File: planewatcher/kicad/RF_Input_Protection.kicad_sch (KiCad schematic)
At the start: 2 parts

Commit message: Add persistent PCBWay BOM fields to KiCad schematic
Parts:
- D3: MPN (none) -> ESD103B102ELE6327XTMA1; Manufacturer (none) -> Infineon; Package (none) -> PG-TSLP-2-20
- L12: MPN (none) -> 0402DC-68NXJRW; Manufacturer (none) -> Coilcraft; Package (none) -> 0402
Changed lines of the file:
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@@
+			)
+		)
+		(property "Package" "PG-TSLP-2-20"
+			(at 139.7 97.79 0)
+			(hide yes)
+			(show_name no)
+			(do_not_autoplace no)
+			(effects
+				(font
+					(size 1.27 1.27)
+				)
+			)
+		)
+		(property "MPN" "ESD103B102ELE6327XTMA1"
+			(at 139.7 97.79 0)
+			(hide yes)
+			(show_name no)
+			(do_not_autoplace no)
+			(effects
+				(font
+					(size 1.27 1.27)
+				)
+			)
+		)
+		(property "Manufacturer" "Infineon"
+			(at 139.7 97.79 0)
+			(hide yes)
+			(show_name no)
+			(do_not_autoplace no)
+			(effects
+				(font
+					(size 1.27 1.27)
+				)
 			)
 		)
@@
 			(at 123.19 97.79 0)
 			(hide yes)
+			(show_name no)
+			(do_not_autoplace no)
+			(effects
+				(font
+					(size 1.27 1.27)
+				)
+			)
+		)
+		(property "Package" "0402"
+			(at 123.19 97.79 0)
+			(hide yes)
+			(show_name no)
+			(do_not_autoplace no)
+			(effects
+				(font
+					(size 1.27 1.27)
+				)
+			)
+		)
+		(property "MPN" "0402DC-68NXJRW"
+			(at 123.19 97.79 0)
+			(hide yes)
+			(show_name no)
+			(do_not_autoplace no)
+			(effects
+				(font
+					(size 1.27 1.27)
+				)
+			)
+		)
+		(property "Manufacturer" "Coilcraft"
+			(at 123.19 97.79 0)
+			(hide yes)

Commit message: move power supply and add GPS module
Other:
- title: Plane Watcher: RF Input Protection -> Plane Watcher
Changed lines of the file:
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@@
 	(paper "A4")
 	(title_block
-		(title "Plane Watcher: RF Input Protection")
-		(date "2026-05-16")
-		(rev "prototype 1.1")
+		(title "Plane Watcher")
+		(date "2026-05-18")
+		(rev "prototype 1.2")
 		(company "plane.watch")
 	)

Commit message: review & consolidate all capacitors
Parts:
- D3: Suggested Part Infineon ESD103B102ELE6327XTMA1 -> (none)
- L12: Suggested Part Coilcraft 0402DC-68NXJRW -> (none)
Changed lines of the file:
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@@
-			)
-		)
-		(property "Suggested Part" "Infineon ESD103B102ELE6327XTMA1"
-			(at 139.7 97.79 0)
-			(hide yes)
-			(show_name no)
-			(do_not_autoplace no)
-			(effects
-				(font
-					(size 1.27 1.27)
-				)
 			)
 		)
@@
 		)
 		(property "Notes" ""
+			(at 139.7 97.79 90)
+			(hide yes)
+			(show_name no)
+			(do_not_autoplace no)
+			(effects
+				(font
+					(size 1.27 1.27)
+				)
+			)
+		)
+		(property "Mount_Type" ""
 			(at 139.7 97.79 90)
 			(hide yes)
@@
 			)
 		)
-		(property "Suggested Part" "Coilcraft 0402DC-68NXJRW"
-			(at 123.19 97.79 0)
-			(hide yes)
-			(show_name no)
-			(do_not_autoplace no)
-			(effects
-				(font
-					(size 1.27 1.27)
-				)
-			)
-		)
 		(property "Purpose" "RF choke/shunt inductor to ground; provides DC/static bleed and input matching/filtering at 1090MHz."
 			(at 123.19 97.79 0)
@@
 			(at 123.19 97.79 0)
 			(hide yes)
+			(show_name no)
+			(do_not_autoplace no)
+			(effects
+				(font
+					(size 1.27 1.27)
+				)
+			)
+		)
+		(property "Mount_Type" ""
+			(at 123.19 97.79 0)
+			(hide yes)

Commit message: swap TVS diodes with easier to source part
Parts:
- D3: value ESD103-B1-02EL -> ESD8472MUT5G; footprint planewatcher:D_ESD112-B1-02EL_TSLP-2-20 -> Diode_SMD:D_0201_0603Metric; MPN ESD103B102ELE6327XTMA1 -> ESD8472MUT5G; Manufacturer Infineon -> onsemi; Package PG-TSLP-2-20 -> 2-X3DFN (0.6x0.3) (0201); Purpose Provides low-capacitance ESD protection to chassis/board ground. -> Provides low-capacitance ESD protection to chassis/board ground for 1090MHz RF input.
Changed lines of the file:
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@@
 			)
 		)
-		(property "Value" "ESD103-B1-02EL"
+		(property "Value" "ESD8472MUT5G"
 			(at 142.24 99.0599 90)
 			(show_name no)
@@
 			)
 		)
-		(property "Footprint" "planewatcher:D_ESD112-B1-02EL_TSLP-2-20"
+		(property "Footprint" "Diode_SMD:D_0201_0603Metric"
 			(at 139.7 97.79 0)
 			(hide yes)
@@
 			)
 		)
-		(property "Datasheet" "https://www.infineon.com/cms/en/product/esd-and-surge-protection/low-capacitance-esd-devices/esd103-b1-02el/"
+		(property "Datasheet" "https://www.onsemi.com/download/data-sheet/pdf/esd8472-d.pdf"
 			(at 139.7 97.79 0)
 			(hide yes)
@@
 			)
 		)
-		(property "Description" "Low-capacitance bidirectional RF ESD diode, 0.13pF typical, ±15V working voltage, PG-TSLP-2-20 package"
+		(property "Description" "14V Clamp 3A (8/20µs) Ipp Tvs Diode Surface Mount 2-X3DFN (0.6x0.3) (0201)"
 			(at 139.7 97.79 0)
 			(hide yes)
@@
 			)
 		)
-		(property "Package" "PG-TSLP-2-20"
+		(property "Package" "2-X3DFN (0.6x0.3) (0201)"
 			(at 139.7 97.79 0)
 			(hide yes)
@@
 			)
 		)
-		(property "MPN" "ESD103B102ELE6327XTMA1"
+		(property "MPN" "ESD8472MUT5G"
 			(at 139.7 97.79 0)
 			(hide yes)
@@
 			)
 		)
-		(property "Manufacturer" "Infineon"
+		(property "Manufacturer" "onsemi"
 			(at 139.7 97.79 0)
 			(hide yes)
@@
 			)
 		)
-		(property "Purpose" "Provides low-capacitance ESD protection to chassis/board ground."
+		(property "Purpose" "Provides low-capacitance ESD protection to chassis/board ground for 1090MHz RF input."
 			(at 139.7 97.79 90)
 			(hide yes)

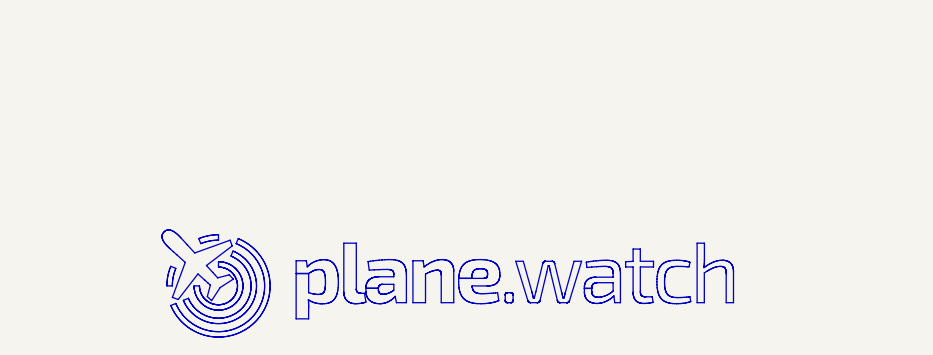
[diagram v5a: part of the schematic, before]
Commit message: add license & copyright info to schematic and pcb. fix layer window.
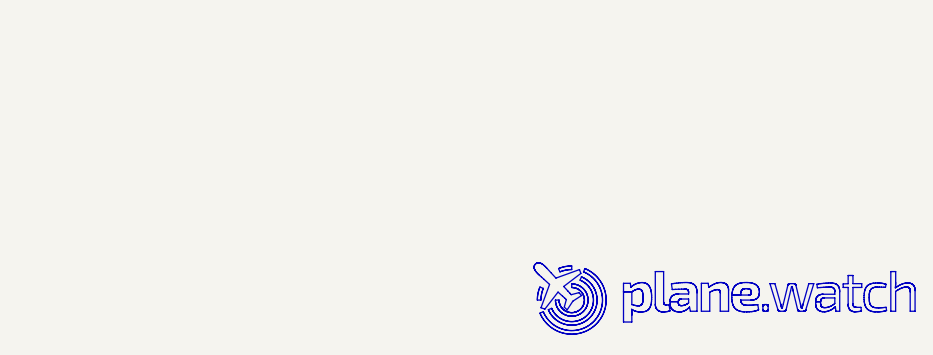
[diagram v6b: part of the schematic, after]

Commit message: added lcsc_ids to all parts
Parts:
- D3: lcsc_id (none) -> C133346
- L12: lcsc_id (none) -> C3221883
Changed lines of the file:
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@@
+			)
+		)
+		(property "lcsc_id" "C133346"
+			(at 139.7 97.79 0)
+			(hide yes)
+			(show_name no)
+			(do_not_autoplace no)
+			(effects
+				(font
+					(size 1.27 1.27)
+				)
 			)
 		)
@@
 			(at 123.19 97.79 0)
 			(hide yes)
+			(show_name no)
+			(do_not_autoplace no)
+			(effects
+				(font
+					(size 1.27 1.27)
+				)
+			)
+		)
+		(property "lcsc_id" "C3221883"
+			(at 123.19 97.79 0)
+			(hide yes)
